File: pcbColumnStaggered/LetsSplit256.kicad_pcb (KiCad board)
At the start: 2 copper layers, 137.2 x 103.5 mm, 63 parts, among them U1 ProMicro

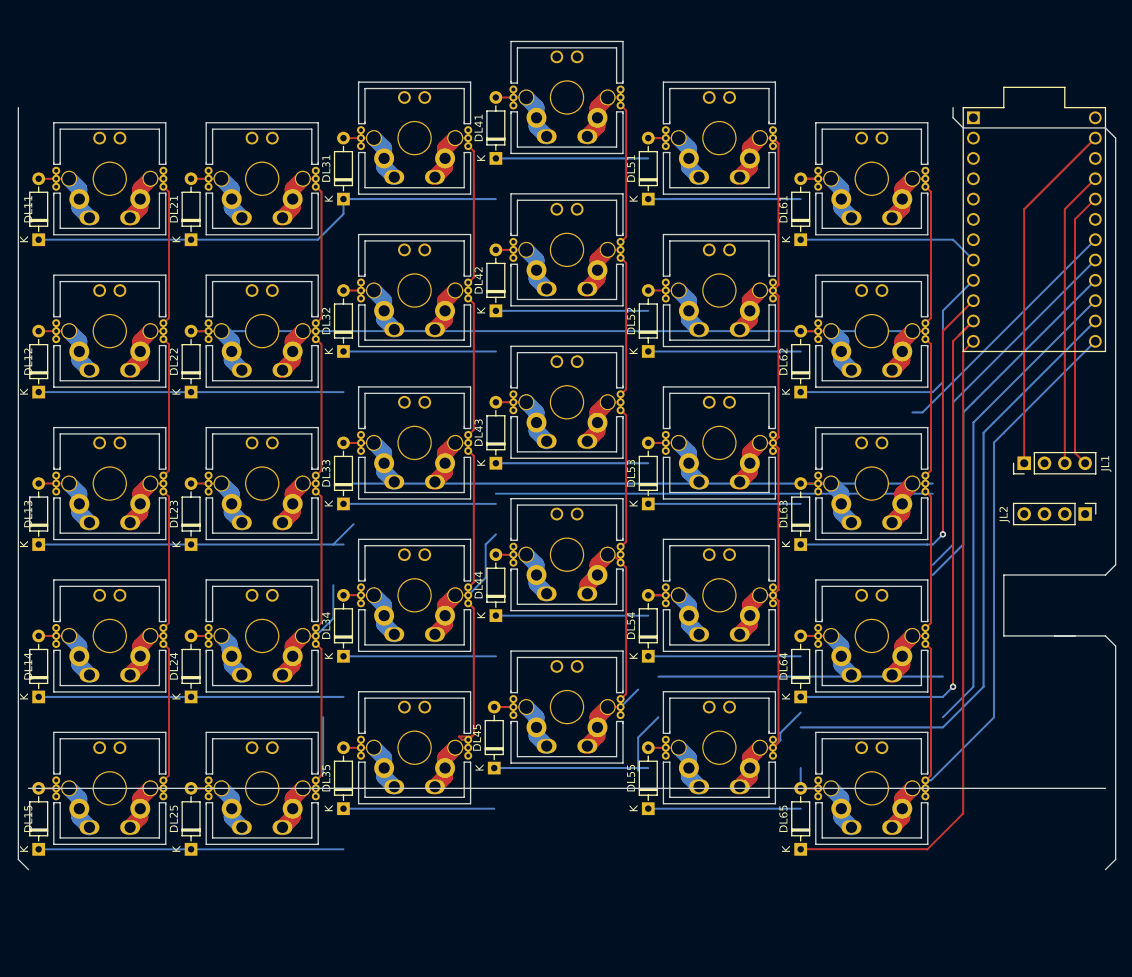
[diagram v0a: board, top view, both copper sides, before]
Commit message: Finalize column staggered version
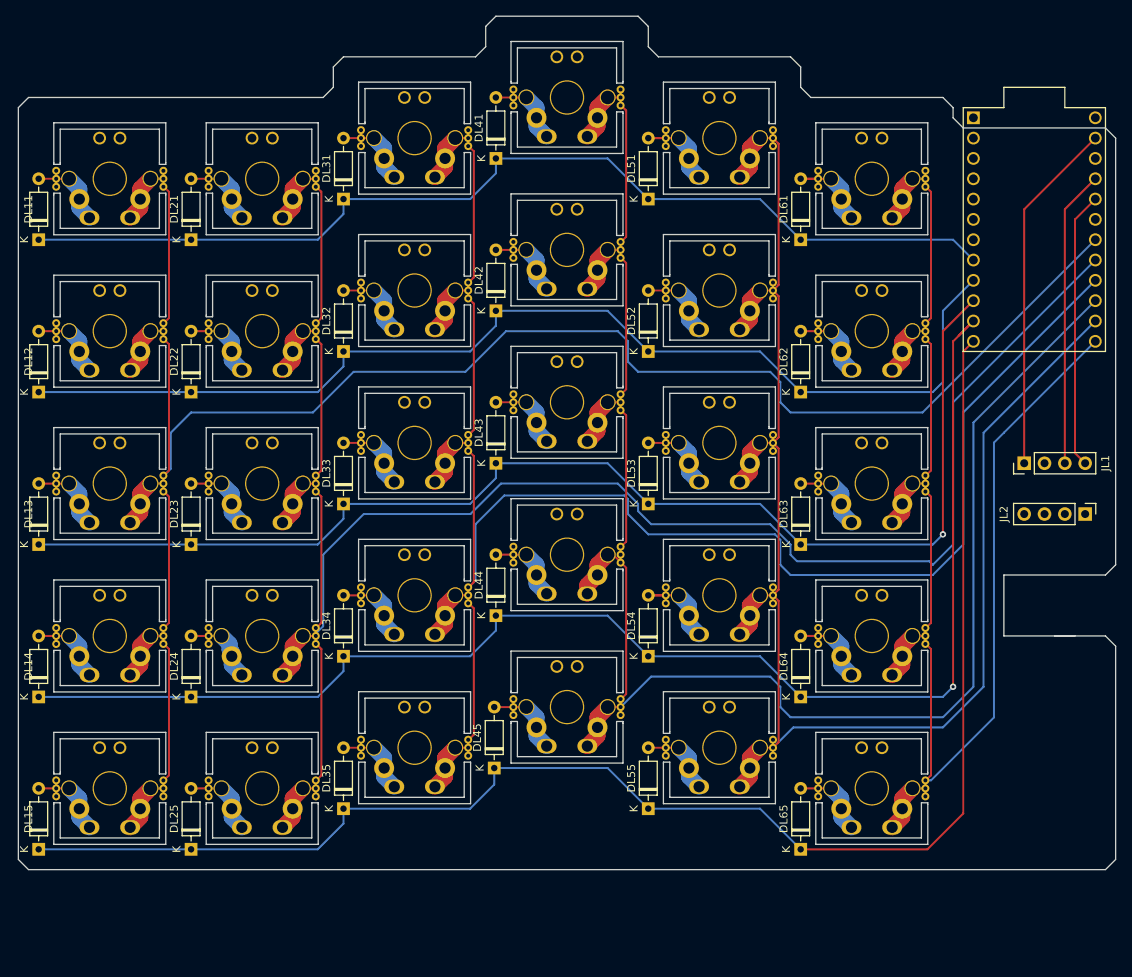
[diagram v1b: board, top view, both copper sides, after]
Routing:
- net Net-(KL1-Pad2): track 180.7 -> 262.1 mm
- net Net-(DL13-Pad1): track 220.3 -> 154.9 mm
- net Net-(KLFunc11-Pad2): track 241.2 -> 261.3 mm
- net Net-(DL15-Pad1): track 177.0 -> 187.7 mm
- net Net-(DL14-Pad1): track 164.2 -> 174.8 mm
- net Net-(DL12-Pad1): track 127.8 -> 138.4 mm
- net Net-(KL2-Pad2): track 229.8 -> 237.8 mm
- net Net-(DL11-Pad1): track 121.1 -> 128.5 mm
- net Net-(DL65-Pad2): track 15.0 -> 11.7 mm
- net Net-(KL4-Pad2): track 208.8 -> 207.5 mm
- net Net-(KL3-Pad2): track 225.2 -> 224.3 mm
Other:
- board size 137.2 x 103.5 mm -> 137.2 x 106.7 mm

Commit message: Update Column Staggered PCB
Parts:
- moved KLFunc65 22.2 mm to (149.9, 133.3)
- moved DL65 22.2 mm to (141.0, 141.0)
- moved DL45 19.9 mm to (102.9, 124.5)
- moved KLFunc45 19.7 mm to (111.8, 116.8)
- moved DL25 19.7 mm to (64.8, 124.5)
- moved DL35 19.7 mm to (83.8, 119.4)
- moved DL55 19.7 mm to (121.9, 129.5)
- moved KLFunc25 19.7 mm to (73.7, 116.8)
- moved KLFunc35 19.7 mm to (92.7, 111.8)
- moved KLFunc55 19.7 mm to (130.8, 121.9)
- moved DL15 19.0 mm to (45.7, 129.5)
- moved KLFunc15 19.0 mm to (54.6, 121.9)
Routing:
- net Net-(KLFunc11-Pad2): track 261.3 -> 279.6 mm
- net Net-(KL5-Pad2): track 183.9 -> 200.7 mm, vias 0 -> 1
- net Net-(KL1-Pad2): track 262.1 -> 276.3 mm
- net Net-(KL2-Pad2): track 237.8 -> 250.9 mm
- net Net-(DL15-Pad1): track 187.7 -> 182.7 mm
- net Net-(KL3-Pad2): track 224.3 -> 225.3 mm
- net Net-(KL4-Pad2): track 207.5 -> 208.4 mm, vias 0 -> 1
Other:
- board size 137.2 x 106.7 mm -> 137.2 x 118.1 mm

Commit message: Generate geber
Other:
- outline, holes or cut-outs redrawn

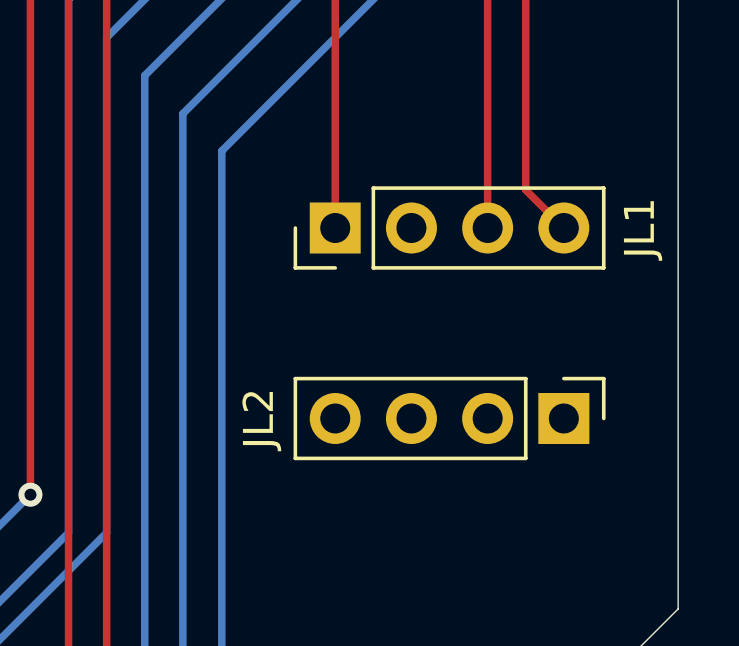
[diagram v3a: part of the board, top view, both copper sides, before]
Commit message: Remove unnecessary jumpers for 3.5mm ports
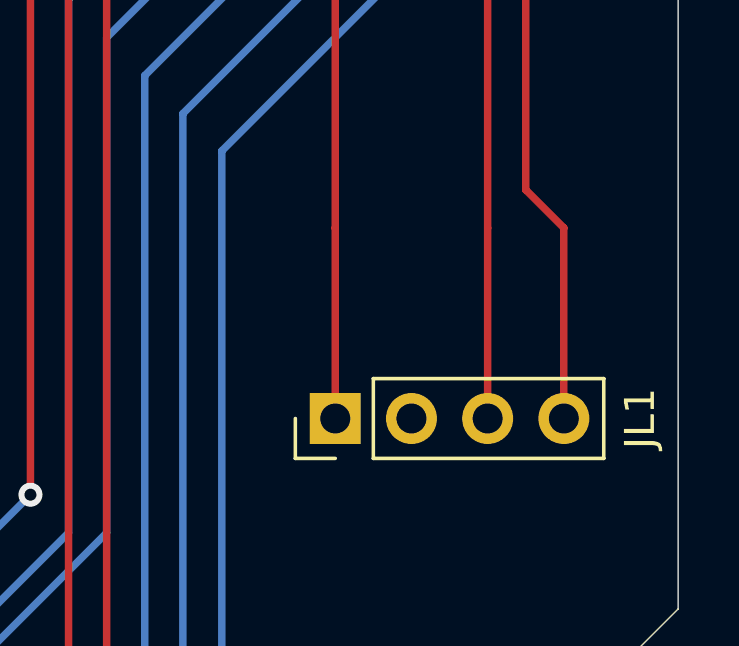
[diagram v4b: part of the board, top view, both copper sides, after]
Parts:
- removed JL2: Conn_01x04, Connector_PinHeader_2.54mm:PinHeader_1x04_P2.54mm_Vertical
- moved JL1 6.35 mm to (149.9, 87.6)
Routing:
- net Net-(JL1-Pad4): track 34.6 -> 40.9 mm
- net Net-(JL1-Pad3): track 37.1 -> 43.5 mm
- net Net-(JL1-Pad1): track 44.3 -> 50.7 mm
